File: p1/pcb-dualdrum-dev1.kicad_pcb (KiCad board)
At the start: 2 copper layers, 48 x 109.2 mm, 152 parts, among them P1 CONN-02x05, U1 082, U2 082, U3 082, U4 082, U5 082, U6 082, U7 082, U8 082-NJM, U9 082

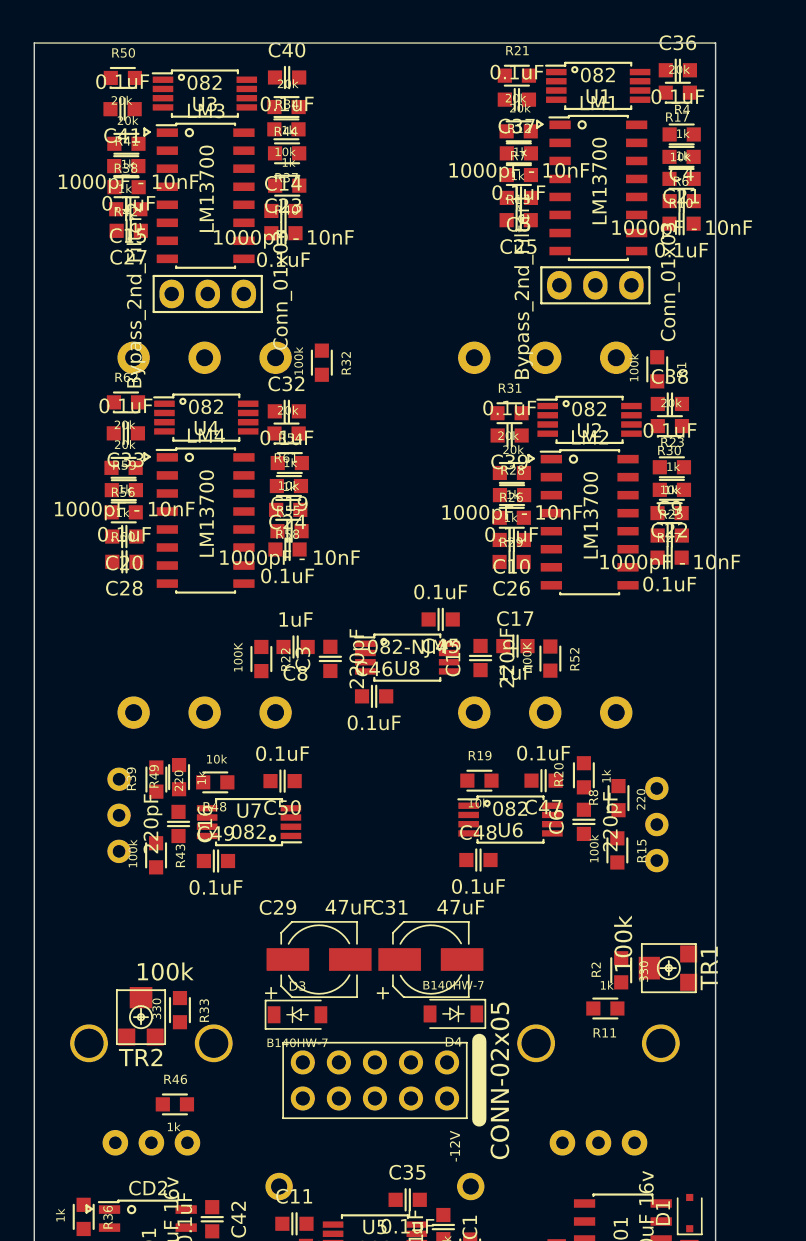
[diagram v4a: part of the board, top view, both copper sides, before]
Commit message: created fp file - ready to layout dev board
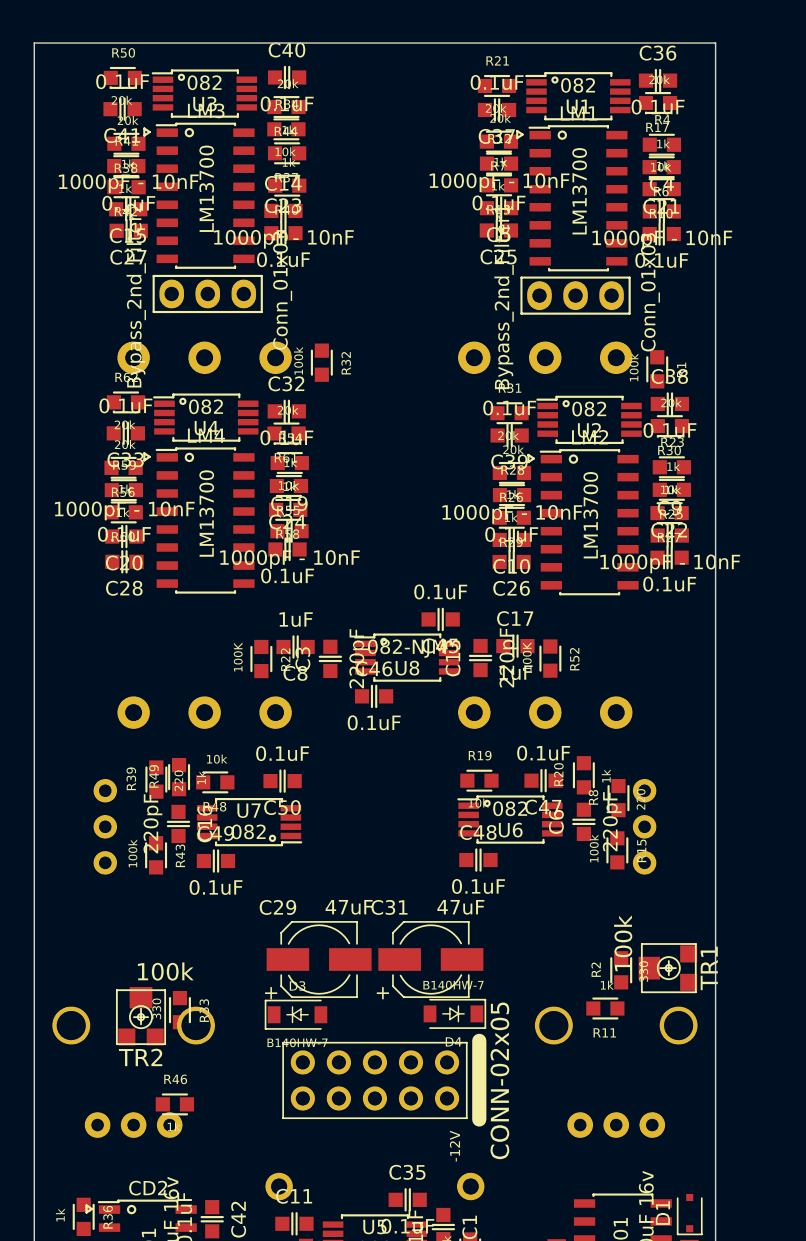
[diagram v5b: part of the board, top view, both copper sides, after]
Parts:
- moved Gate_PW1 1.77 mm to (41.0, -40.0)
- moved Gate_PW2 1.77 mm to (7.00, -40.0)
- moved Bypass_2nd_Filter1 1.57 mm to (38.1, -91.4)
- moved C25 1.57 mm to (32.7, -96.0)
- moved C36 1.57 mm to (43.9, -106.6)
- moved C37 1.57 mm to (32.6, -104.5)
- moved LM1 1.57 mm to (38.3, -98.3)
- moved R10 1.57 mm to (44.2, -98.9)
- moved R17 1.57 mm to (43.9, -105.0)
- moved R7 1.57 mm to (32.7, -102.3)
- moved C21 1.57 mm to (44.2, -95.8)
- moved C4 1.57 mm to (44.2, -97.4)
- moved C5 1.57 mm to (32.7, -97.6)
- moved R12 1.57 mm to (32.7, -100.7)
- moved R13 1.57 mm to (32.7, -99.2)
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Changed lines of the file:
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@@
   )
   (module 4ms_Package_SSOP:TSSOP-8_4.4x3mm_Pitch0.65mm (layer F.Cu)
-    (at 39.73 -106.2)
+    (at 38.333 -105.47356)
     (descr "8-Lead Plastic Thin Shrink Small Outline (ST)-4.4 mm Body [TSSOP] (see Microchip Packaging Specification 00000049BS.pdf)")
     (tags "SSOP 0.65")
@@
   )
   (module 4ms_Resistor:R_0603 (layer F.Cu)
-    (at 34 -106.92 180)
+    (at 32.603 -106.19356 180)
     (descr "Resistor SMD 0603, reflow soldering, Vishay (see dcrcw.pdf)")
     (tags "resistor 0603")
@@
   )
   (module 4ms_Resistor:R_0603 (layer F.Cu)
-    (at 45.34 -105.72)
+    (at 43.943 -104.99356)
     (descr "Resistor SMD 0603, reflow soldering, Vishay (see dcrcw.pdf)")
     (tags "resistor 0603")
@@
   )
   (module 4ms_Resistor:R_0603 (layer F.Cu)
-    (at 34.14 -99.92)
+    (at 32.743 -99.19356)
     (descr "Resistor SMD 0603, reflow soldering, Vishay (see dcrcw.pdf)")
     (tags "resistor 0603")
@@
   )
   (module 4ms_Resistor:R_0603 (layer F.Cu)
-    (at 34.14 -101.45 180)
+    (at 32.743 -100.72356 180)
     (descr "Resistor SMD 0603, reflow soldering, Vishay (see dcrcw.pdf)")
     (tags "resistor 0603")
@@
   )
   (module 4ms_Resistor:R_0603 (layer F.Cu)
-    (at 45.6 -99.65)
+    (at 44.203 -98.92356)
     (descr "Resistor SMD 0603, reflow soldering, Vishay (see dcrcw.pdf)")
     (tags "resistor 0603")
@@
   )
   (module 4ms_Resistor:R_0603 (layer F.Cu)
-    (at 34.13 -103)
+    (at 32.733 -102.27356)
     (descr "Resistor SMD 0603, reflow soldering, Vishay (see dcrcw.pdf)")
     (tags "resistor 0603")
@@
   )
   (module 4ms_Resistor:R_0603 (layer F.Cu)
-    (at 45.6 -101.2)
+    (at 44.203 -100.47356)
     (descr "Resistor SMD 0603, reflow soldering, Vishay (see dcrcw.pdf)")
     (tags "resistor 0603")
@@
   )
   (module 4ms_Resistor:R_0603 (layer F.Cu)
-    (at 45.61 -102.78 180)
+    (at 44.213 -102.05356 180)
     (descr "Resistor SMD 0603, reflow soldering, Vishay (see dcrcw.pdf)")
     (tags "resistor 0603")
@@
   )
   (module 4ms_Package_SOIC:SOIC-16_3.9x9.9mm_Pitch1.27mm (layer F.Cu)
-    (at 39.74 -99.01)
+    (at 38.343 -98.28356)
     (descr "16-Lead Plastic Small Outline (SL) - Narrow, 3.90 mm Body [SOIC] (see Microchip Packaging Specification 00000049BS.pdf)")
     (tags "SOIC 1.27")
@@
   )
   (module 4ms_Capacitor:C_0603 (layer F.Cu)
-    (at 34 -105.23 180)
+    (at 32.603 -104.50356 180)
     (descr "Capacitor SMD 0603, reflow soldering, AVX (see smccp.pdf)")
     (tags "capacitor 0603 C0603")
@@
   )
   (module 4ms_Capacitor:C_0603 (layer F.Cu)
-    (at 45.34 -107.3)
+    (at 43.943 -106.57356)
     (descr "Capacitor SMD 0603, reflow soldering, AVX (see smccp.pdf)")
     (tags "capacitor 0603 C0603")
@@
   )
   (module 4ms_Capacitor:C_0603 (layer F.Cu)
-    (at 34.13 -96.74 180)
+    (at 32.733 -96.01356 180)
     (descr "Capacitor SMD 0603, reflow soldering, AVX (see smccp.pdf)")
     (tags "capacitor 0603 C0603")
@@
   )
   (module 4ms_Capacitor:C_0603 (layer F.Cu)
-    (at 45.6 -96.49)
+    (at 44.203 -95.76356)
     (descr "Capacitor SMD 0603, reflow soldering, AVX (see smccp.pdf)")
     (tags "capacitor 0603 C0603")
@@
   )
   (module 4ms_Capacitor:C_0603 (layer F.Cu)
-    (at 34.14 -98.31 180)
+    (at 32.743 -97.58356 180)
     (descr "Capacitor SMD 0603, reflow soldering, AVX (see smccp.pdf)")
     (tags "capacitor 0603 C0603")
@@
   )
   (module 4ms_Capacitor:C_0603 (layer F.Cu)
-    (at 45.61 -98.08)
+    (at 44.213 -97.35356)
     (descr "Capacitor SMD 0603, reflow soldering, AVX (see smccp.pdf)")
     (tags "capacitor 0603 C0603")
@@
   )
   (module 4ms_Connector:Pins_1x03_2.54mm_TH (layer F.Cu)
-    (at 39.53 -92.15 90)
+    (at 38.133 -91.42356 90)
     (descr "Through hole pin header")
     (tags "pin header")
@@
   )
   (module 4ms_Switch:Switch_Toggle_SPDT_SubMini (layer B.Cu)
-    (at 5.97 -54.81)
+    (at 5 -54)
     (fp_text reference MIC/LINE2 (at -1.88 4.4) (layer B.SilkS)
       (effects (font (size 1 1) (thickness 0.15)) (justify right bottom mirror))
@@
   )
   (module 4ms_Switch:Switch_Toggle_SPDT_SubMini (layer B.Cu)
-    (at 43.86 -54.16)
+    (at 43 -54)
     (fp_text reference MIC/LINE1 (at -1.88 4.4) (layer B.SilkS)
       (effects (font (size 1 1) (thickness 0.15)) (justify right bottom mirror))
@@
   )
   (module 4ms_Potentiometer:Pot_9mm_Knurl_NoDet (layer B.Cu)
-    (at 8.25 -38.75)
+    (at 7 -40)
     (fp_text reference Gate_PW2 (at -4.6 4.1) (layer B.SilkS)
       (effects (font (size 1 1) (thickness 0.15)) (justify right bottom mirror))
@@
   )
   (module 4ms_Potentiometer:Pot_9mm_Knurl_NoDet (layer B.Cu)
-    (at 39.75 -38.75)
+    (at 41 -40)
     (fp_text reference Gate_PW1 (at -4.6 4.1) (layer B.SilkS)
       (effects (font (size 1 1) (thickness 0.15)) (justify right bottom mirror))

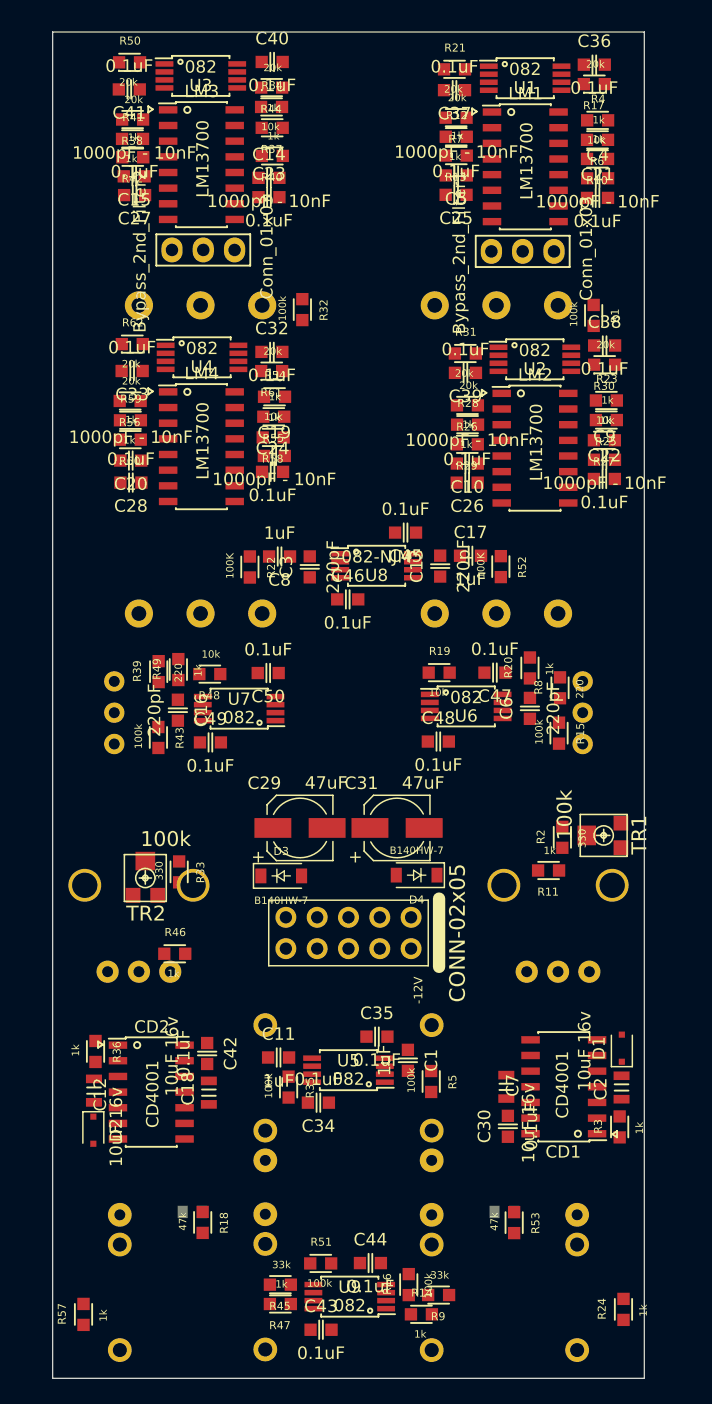
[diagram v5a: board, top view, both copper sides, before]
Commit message: beginning to lay tracks
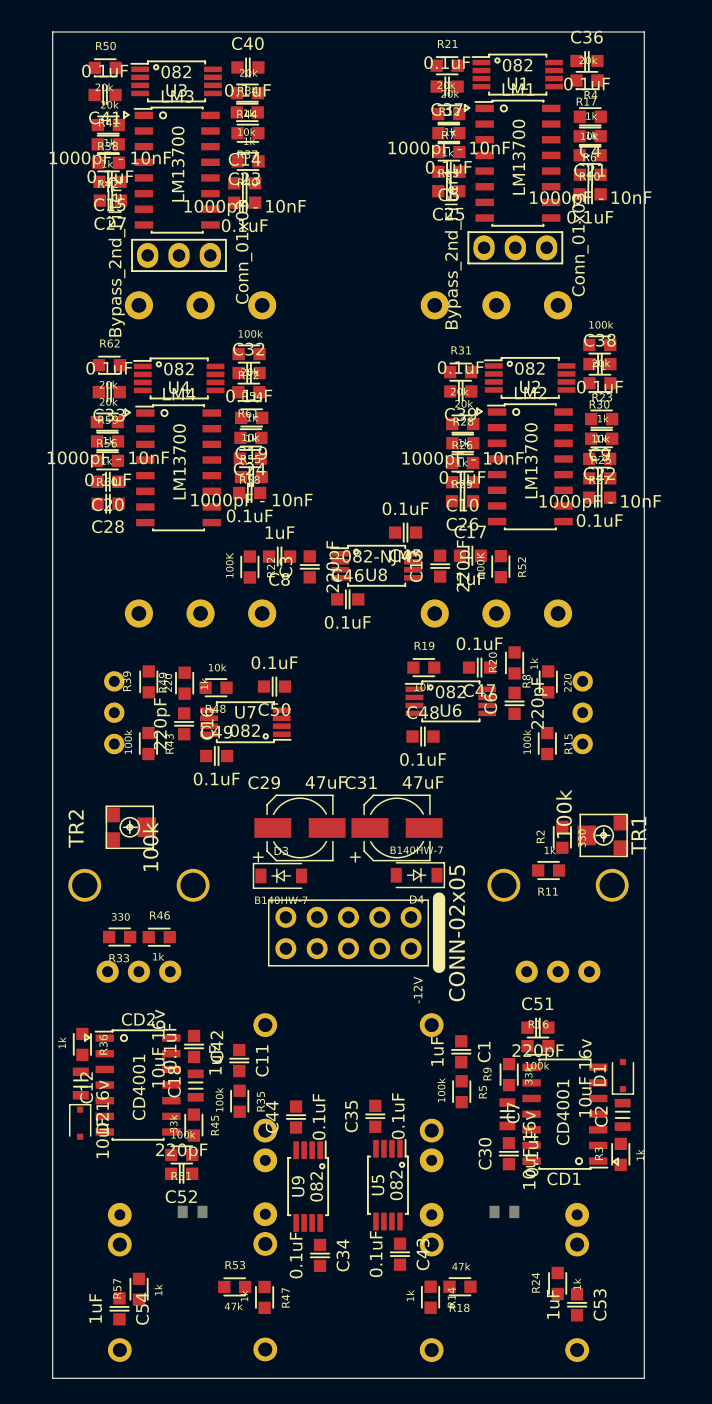
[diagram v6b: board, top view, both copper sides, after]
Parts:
- added C51: 220pF, 4ms_Capacitor:C_0603, F.Cu at (39.4, -28.4)
- added C52: 220pF, 4ms_Capacitor:C_0603, F.Cu at (10.5, -16.6)
- added C53: 1uF, 4ms_Capacitor:C_0603, F.Cu at (42.5, -5.97)
- added C54: 1uF, 4ms_Capacitor:C_0603, F.Cu at (5.42, -5.64)
- moved GATE_LED1 25.3 mm to (36.6, -13.5)
- moved GATE_LED2 25.3 mm to (11.3, -13.5)
- moved R53 23.3 mm to (14.8, -7.42), turned to 180 degrees
- moved R16 22.0 mm to (39.4, -26.9), turned to 180 degrees
- moved R18 21.5 mm to (33.0, -7.43), turned to 0 degrees
- moved R9 18.8 mm to (37.0, -24.6), turned to 270 degrees
- moved R45 14.7 mm to (11.5, -20.5), turned to 90 degrees
- moved R51 14.3 mm to (10.5, -18.1), turned to 0 degrees
- moved C44 13.3 mm to (19.7, -21.2), turned to 90 degrees
- moved C34 12.4 mm to (21.7, -9.97), turned to 270 degrees
- moved U5 9.86 mm to (27.2, -15.7), turned to 270 degrees
- moved U9 9.55 mm to (20.7, -15.6), turned to 270 degrees
- moved C43 8.87 mm to (28.2, -10.1), turned to 270 degrees
- moved R33 7.16 mm to (5.44, -35.8), turned to 0 degrees
- moved C35 6.46 mm to (26.2, -21.3), turned to 90 degrees
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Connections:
- R16 pad 2: Net-(R16-Pad2) -> Net-(C51-Pad1)
- R24 pad 2: Net-(AUDIO_OUT1-Pad1) -> Net-(C53-Pad1)
- R57 pad 2: Net-(AUDIO_OUT2-Pad1) -> Net-(C54-Pad1)
- R9 pad 1: Net-(R16-Pad2) -> Net-(C51-Pad1)
- U5 pad 5: Net-(C11-Pad2) -> Net-(C51-Pad1)
- U5 pad 6: Net-(R34-Pad1) -> Net-(R14-Pad2)
- U5 pad 7: Net-(R34-Pad1) -> Net-(R14-Pad2)
- U9 pad 1: Net-(R14-Pad2) -> Net-(R34-Pad1)
- U9 pad 2: Net-(R14-Pad2) -> Net-(R34-Pad1)
- U9 pad 3: Net-(R16-Pad2) -> Net-(C11-Pad2)

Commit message: finished pwr and gnd tracks
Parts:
- moved R22 28.4 mm to (44.0, -61.3), turned to 270 degrees
- moved C8 26.0 mm to (43.2, -58.9), turned to 0 degrees
- moved C13 21.1 mm to (11.5, -58.8), turned to 0 degrees
- moved C3 20.2 mm to (39.9, -58.9), turned to 0 degrees
- moved R52 20.2 mm to (16.2, -66.8), turned to 180 degrees
- moved C17 17.8 mm to (16.2, -65.3), turned to 180 degrees
- moved C45 14.7 mm to (43.3, -68.1), turned to 0 degrees
- moved U8 11.4 mm to (37.7, -67.0)
- moved C31 9.09 mm to (27.5, -35.6), turned to 270 degrees
- moved D4 8.98 mm to (23.7, -34.0), turned to 270 degrees
- moved C46 8.55 mm to (32.1, -65.9), turned to 180 degrees
- moved C29 7.57 mm to (27.5, -43.4), turned to 270 degrees
- moved R2 7.41 mm to (39.4, -36.7), turned to 0 degrees
- moved D3 6.62 mm to (23.7, -45.0), turned to 270 degrees
- moved P1 6.02 mm to (19.0, -39.5), turned to 0 degrees
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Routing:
- net GND: track 0.00 -> 538.2 mm, vias 0 -> 32
- net +12V: track 0.00 -> 393.2 mm, vias 0 -> 21
- net -12VA: track 0.00 -> 273.1 mm, vias 0 -> 14
- net Net-(D4-Pad1): track 0.00 -> 6.46 mm
- net Net-(D3-Pad2): track 0.00 -> 6.43 mm
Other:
- net class GND added: clearance 0.2, trace_width 0.35, via_dia 1, via_drill 0.4

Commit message: wip
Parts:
- moved R32 1.23 mm to (15.1, -84.0), turned to 90 degrees
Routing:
- net Net-(R34-Pad1): track 0.00 -> 126.5 mm, vias 0 -> 4
- net Net-(Bypass_2nd_Filter2-Pad1): track 0.00 -> 81.1 mm, vias 0 -> 4
- net Net-(Freq2-Pad2): track 0.00 -> 40.9 mm, vias 0 -> 6
- net Net-(LM4-Pad13): track 0.00 -> 32.1 mm, vias 0 -> 6
- net Net-(LM3-Pad13): track 0.00 -> 31.5 mm, vias 0 -> 5
- net Net-(Bypass_2nd_Filter2-Pad2): track 0.00 -> 29.7 mm, vias 0 -> 3
- net Net-(Bypass_2nd_Filter2-Pad3): track 0.00 -> 24.4 mm, vias 0 -> 3
- net Net-(C6-Pad1): track 0.00 -> 18.6 mm, vias 0 -> 2
- net Net-(C3-Pad2): track 0.00 -> 15.0 mm, vias 0 -> 1
- net Net-(C20-Pad1): track 0.00 -> 12.3 mm
- net Net-(C15-Pad1): track 0.00 -> 11.7 mm
- net Net-(C16-Pad2): track 0.00 -> 11.6 mm, vias 0 -> 2
- net Net-(R48-Pad2): track 0.00 -> 11.6 mm, vias 0 -> 2
- net Net-(C19-Pad1): track 0.00 -> 11.5 mm
- net Net-(C14-Pad1): track 0.00 -> 10.7 mm
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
